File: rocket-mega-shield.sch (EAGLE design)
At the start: 66 parts, among them J1 ExtBatt, J2 Mega R3, J3 XBEE, J4 MICROSD, J5 U.FL, J6 1X6TERMINALBLOCK, Q1 SI7112DN, Q2 BSS138, Q3 BSS138, Q4 SI7112DN, Q5 SI7112DN, Q6 SI7112DN, Q7 SI7112DN, U1 NCP1117DT33G, U2 M74HC4050M, U3 FGPMMOPA6H, U4 BMP180, U5 LSM303DLHCTR, U6 L3GD20TR, U7 ADXL377

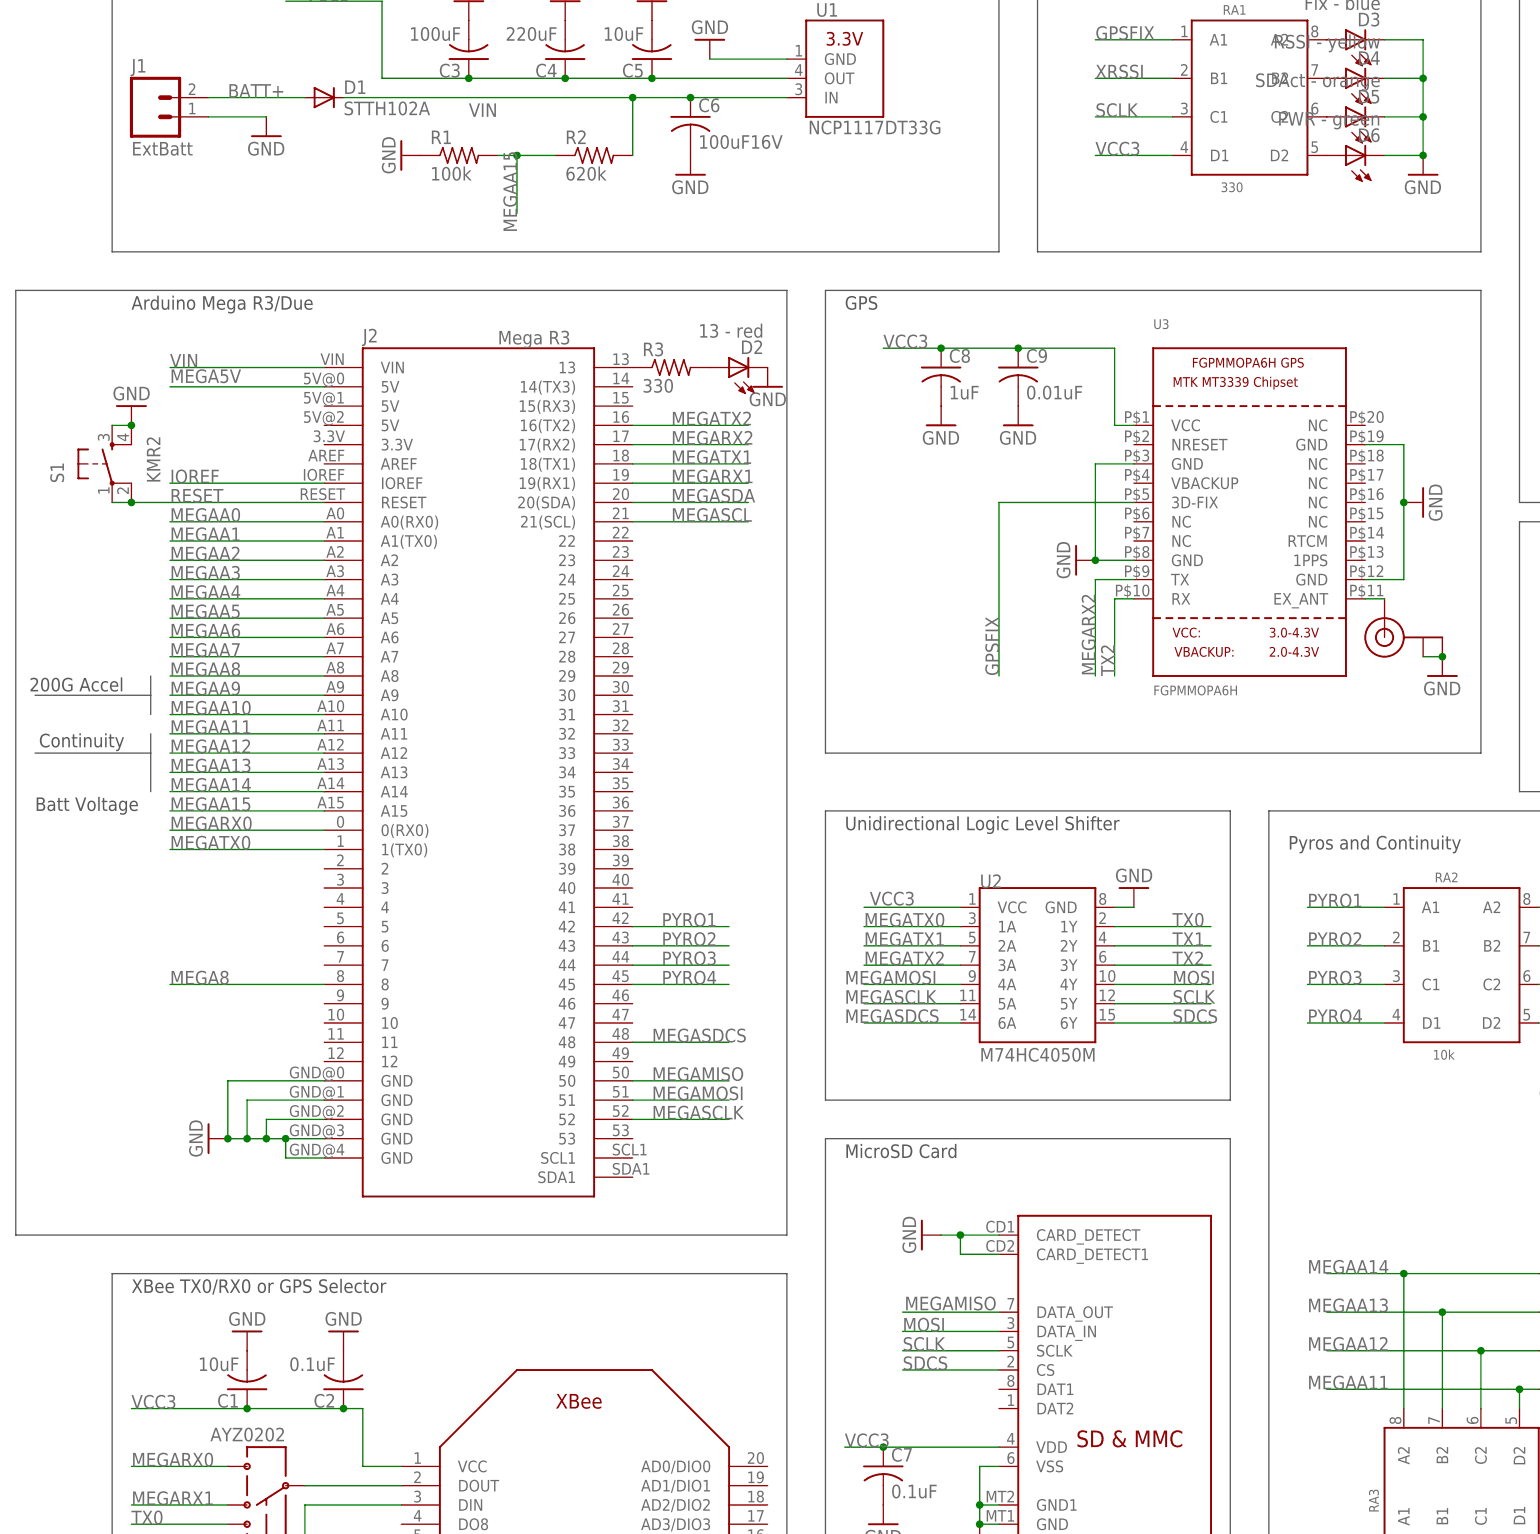
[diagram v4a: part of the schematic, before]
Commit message: moving pins around to match the Due pin availablility
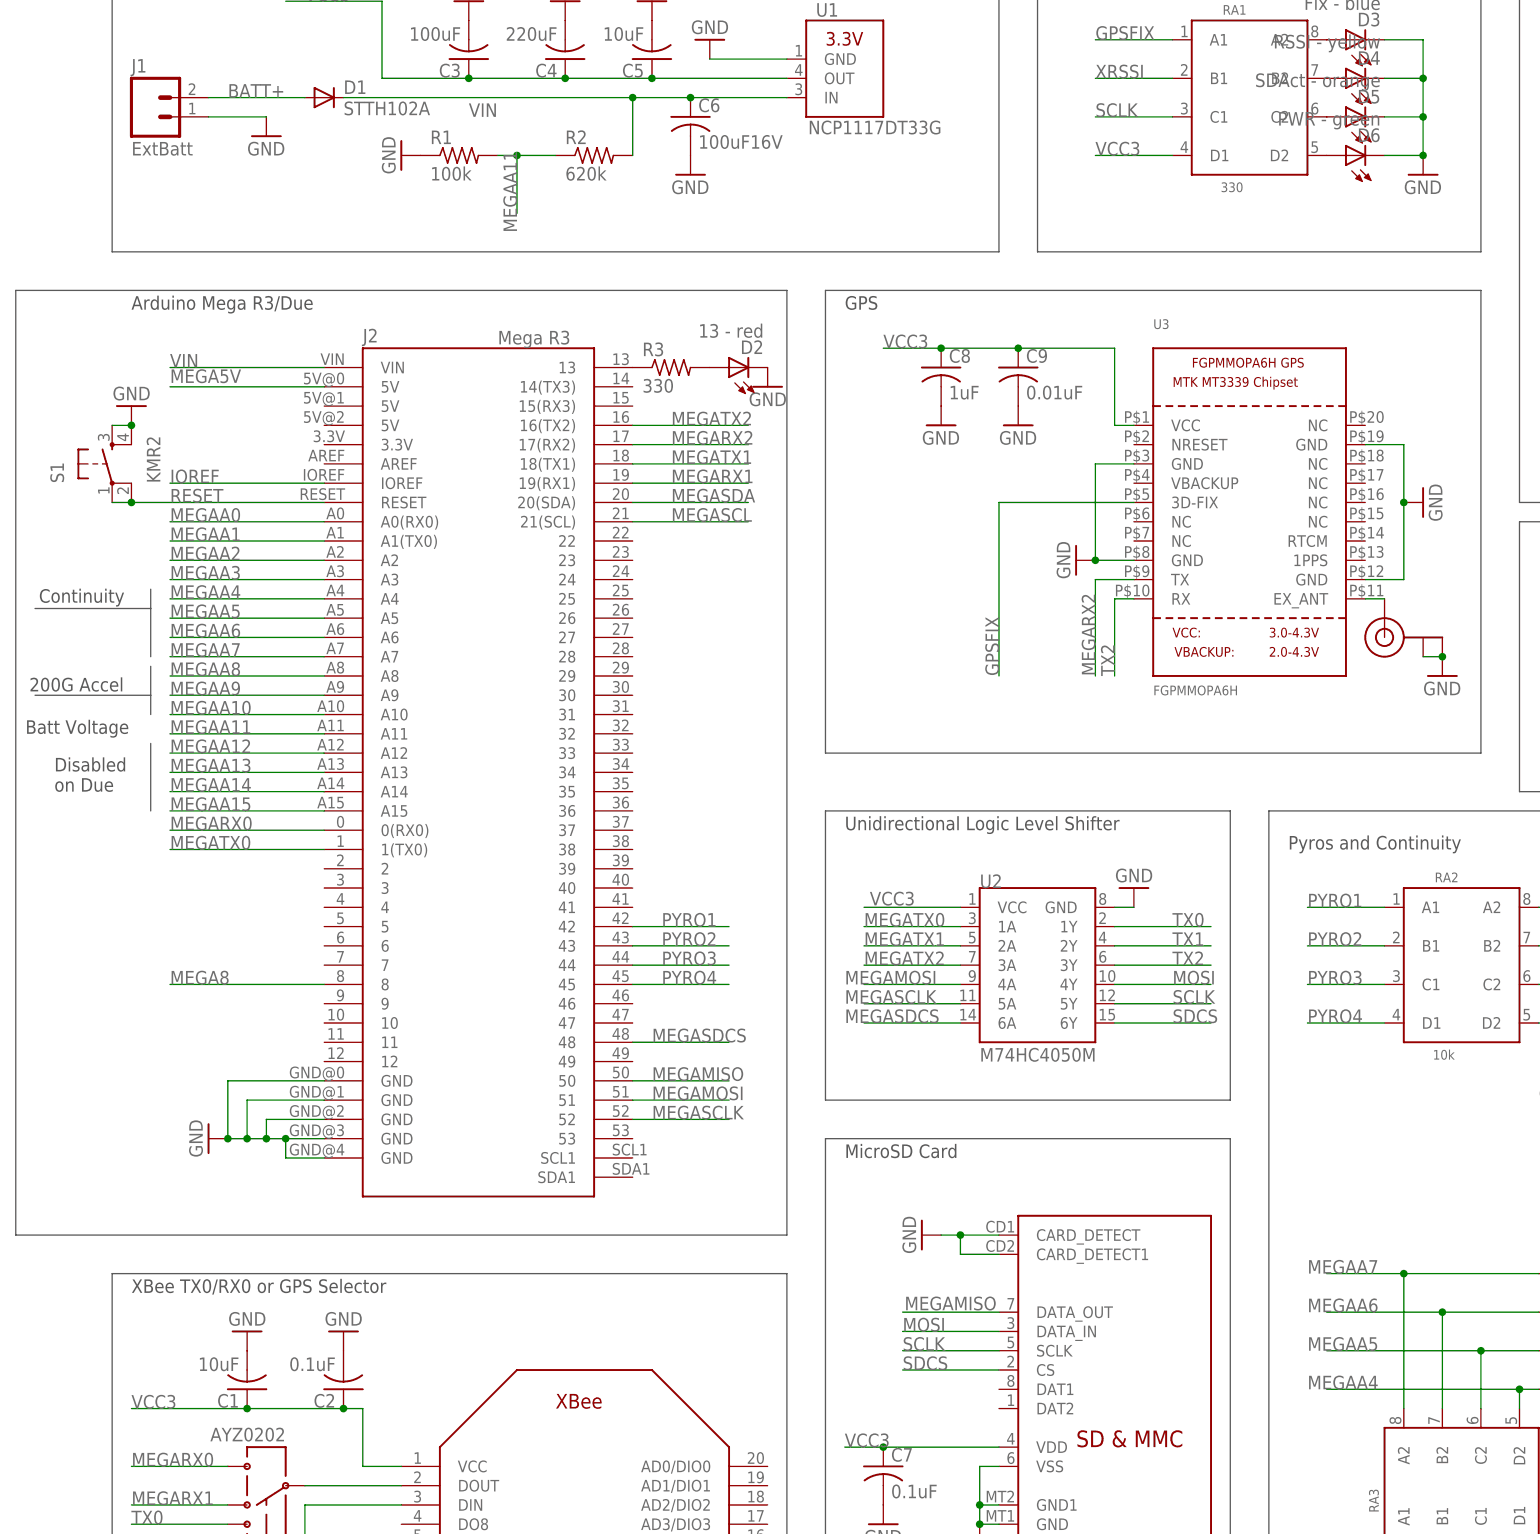
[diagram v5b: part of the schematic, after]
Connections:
- net MEGAA11: now also R1.2, R2.1; no longer RA3.D2, RA4.D1
- net MEGAA12: no longer RA3.C2, RA4.C1
- net MEGAA13: no longer RA3.B2, RA4.B1
- net MEGAA14: no longer RA3.A2, RA4.A1
- net MEGAA15: no longer R1.2, R2.1
- net MEGAA4: now also RA3.D2, RA4.D1
- net MEGAA5: now also RA3.C2, RA4.C1
- net MEGAA6: now also RA3.B2, RA4.B1
- net MEGAA7: now also RA3.A2, RA4.A1
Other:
- note added: "Disabled on Due"
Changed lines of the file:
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@@
 <wire x1="27.94" y1="114.3" x2="-30.48" y2="114.3" width="0.1524" layer="97"/>
 <text x="-27.94" y="109.22" size="1.778" layer="97">LED Bank 1</text>
-<wire x1="-147.32" y1="15.24" x2="-147.32" y2="12.7" width="0.1524" layer="97"/>
+<wire x1="-147.32" y1="16.51" x2="-147.32" y2="12.7" width="0.1524" layer="97"/>
 <wire x1="-147.32" y1="12.7" x2="-147.32" y2="10.16" width="0.1524" layer="97"/>
 <wire x1="-162.56" y1="12.7" x2="-147.32" y2="12.7" width="0.1524" layer="97"/>
 <text x="-163.322" y="13.208" size="1.778" layer="97">200G Accel</text>
-<wire x1="-147.32" y1="7.62" x2="-147.32" y2="5.08" width="0.1524" layer="97"/>
-<wire x1="-147.32" y1="5.08" x2="-147.32" y2="0" width="0.1524" layer="97"/>
-<wire x1="-147.32" y1="5.08" x2="-162.56" y2="5.08" width="0.1524" layer="97"/>
-<text x="-162.052" y="5.842" size="1.778" layer="97">Continuity</text>
-<text x="-162.56" y="-2.54" size="1.778" layer="97">Batt Voltage</text>
+<wire x1="-147.32" y1="26.67" x2="-147.32" y2="24.13" width="0.1524" layer="97"/>
+<wire x1="-147.32" y1="24.13" x2="-147.32" y2="17.78" width="0.1524" layer="97"/>
+<wire x1="-147.32" y1="24.13" x2="-162.56" y2="24.13" width="0.1524" layer="97"/>
+<text x="-162.052" y="24.892" size="1.778" layer="97">Continuity</text>
+<text x="-163.83" y="7.62" size="1.778" layer="97">Batt Voltage</text>
 <text x="35.56" y="33.02" size="1.778" layer="97">Buzzer</text>
 <wire x1="33.02" y1="35.56" x2="33.02" y2="0" width="0.1524" layer="97"/>
@@
 <text x="-140.97" y="121.92" size="1.778" layer="97" font="vector">Designed by Kurtis Kopf</text>
 <text x="-140.97" y="119.38" size="1.778" layer="97" font="vector">OpenSourceAerospace.com</text>
+<wire x1="-147.32" y1="6.35" x2="-147.32" y2="-2.54" width="0.1524" layer="97"/>
+<text x="-160.02" y="0" size="1.778" layer="97">Disabled
+on Due</text>
 </plain>
 <instances>
@@
 <label x="-144.78" y="25.4" size="1.778" layer="95"/>
 </segment>
+<segment>
+<pinref part="RA4" gate="G$1" pin="D1"/>
+<wire x1="35.56" y1="-78.74" x2="33.02" y2="-78.74" width="0.1524" layer="91"/>
+<pinref part="RA3" gate="G$1" pin="D2"/>
+<wire x1="33.02" y1="-78.74" x2="7.62" y2="-78.74" width="0.1524" layer="91"/>
+<wire x1="33.02" y1="-81.28" x2="33.02" y2="-78.74" width="0.1524" layer="91"/>
+<junction x="33.02" y="-78.74"/>
+<label x="5.08" y="-78.74" size="1.778" layer="95"/>
+</segment>
 </net>
 <net name="MEGAA5" class="0">
@@
 <label x="-144.78" y="22.86" size="1.778" layer="95"/>
 </segment>
+<segment>
+<pinref part="RA4" gate="G$1" pin="C1"/>
+<wire x1="35.56" y1="-73.66" x2="27.94" y2="-73.66" width="0.1524" layer="91"/>
+<pinref part="RA3" gate="G$1" pin="C2"/>
+<wire x1="27.94" y1="-73.66" x2="7.62" y2="-73.66" width="0.1524" layer="91"/>
+<wire x1="27.94" y1="-81.28" x2="27.94" y2="-73.66" width="0.1524" layer="91"/>
+<junction x="27.94" y="-73.66"/>
+<label x="5.08" y="-73.66" size="1.778" layer="95"/>
+</segment>
 </net>
 <net name="MEGAA6" class="0">
@@
 <wire x1="-124.46" y1="20.32" x2="-144.78" y2="20.32" width="0.1524" layer="91"/>
 <label x="-144.78" y="20.32" size="1.778" layer="95"/>
+</segment>
+<segment>
+<pinref part="RA4" gate="G$1" pin="B1"/>
+<wire x1="35.56" y1="-68.58" x2="22.86" y2="-68.58" width="0.1524" layer="91"/>
+<pinref part="RA3" gate="G$1" pin="B2"/>
+<wire x1="22.86" y1="-68.58" x2="7.62" y2="-68.58" width="0.1524" layer="91"/>
+<wire x1="22.86" y1="-81.28" x2="22.86" y2="-68.58" width="0.1524" layer="91"/>
+<junction x="22.86" y="-68.58"/>
+<label x="5.08" y="-68.58" size="1.778" layer="95"/>
 </segment>
 </net>
@@
 <wire x1="-124.46" y1="17.78" x2="-144.78" y2="17.78" width="0.1524" layer="91"/>
 <label x="-144.78" y="17.78" size="1.778" layer="95"/>
+</segment>
+<segment>
+<pinref part="RA4" gate="G$1" pin="A1"/>
+<wire x1="35.56" y1="-63.5" x2="17.78" y2="-63.5" width="0.1524" layer="91"/>
+<pinref part="RA3" gate="G$1" pin="A2"/>
+<wire x1="17.78" y1="-63.5" x2="7.62" y2="-63.5" width="0.1524" layer="91"/>
+<wire x1="17.78" y1="-81.28" x2="17.78" y2="-63.5" width="0.1524" layer="91"/>
+<junction x="17.78" y="-63.5"/>
+<label x="5.08" y="-63.5" size="1.778" layer="95"/>
 </segment>
 </net>
@@
 </segment>
 <segment>
-<pinref part="RA4" gate="G$1" pin="D1"/>
-<wire x1="35.56" y1="-78.74" x2="33.02" y2="-78.74" width="0.1524" layer="91"/>
-<pinref part="RA3" gate="G$1" pin="D2"/>
-<wire x1="33.02" y1="-78.74" x2="7.62" y2="-78.74" width="0.1524" layer="91"/>
-<wire x1="33.02" y1="-81.28" x2="33.02" y2="-78.74" width="0.1524" layer="91"/>
-<junction x="33.02" y="-78.74"/>
-<label x="5.08" y="-78.74" size="1.778" layer="95"/>
-</segment>
-</net>
-<net name="MEGAA12" class="0">
-<segment>
-<pinref part="J2" gate="G$1" pin="A12"/>
-<wire x1="-124.46" y1="5.08" x2="-144.78" y2="5.08" width="0.1524" layer="91"/>
-<label x="-144.78" y="5.08" size="1.778" layer="95"/>
-</segment>
-<segment>
-<pinref part="RA4" gate="G$1" pin="C1"/>
-<wire x1="35.56" y1="-73.66" x2="27.94" y2="-73.66" width="0.1524" layer="91"/>
-<pinref part="RA3" gate="G$1" pin="C2"/>
-<wire x1="27.94" y1="-73.66" x2="7.62" y2="-73.66" width="0.1524" layer="91"/>
-<wire x1="27.94" y1="-81.28" x2="27.94" y2="-73.66" width="0.1524" layer="91"/>
-<junction x="27.94" y="-73.66"/>
-<label x="5.08" y="-73.66" size="1.778" layer="95"/>
-</segment>
-</net>
-<net name="MEGAA13" class="0">
-<segment>
-<pinref part="J2" gate="G$1" pin="A13"/>
-<wire x1="-124.46" y1="2.54" x2="-144.78" y2="2.54" width="0.1524" layer="91"/>
-<label x="-144.78" y="2.54" size="1.778" layer="95"/>
-</segment>
-<segment>
-<pinref part="RA4" gate="G$1" pin="B1"/>
-<wire x1="35.56" y1="-68.58" x2="22.86" y2="-68.58" width="0.1524" layer="91"/>
-<pinref part="RA3" gate="G$1" pin="B2"/>
-<wire x1="22.86" y1="-68.58" x2="7.62" y2="-68.58" width="0.1524" layer="91"/>
-<wire x1="22.86" y1="-81.28" x2="22.86" y2="-68.58" width="0.1524" layer="91"/>
-<junction x="22.86" y="-68.58"/>
-<label x="5.08" y="-68.58" size="1.778" layer="95"/>
-</segment>
-</net>
-<net name="MEGAA14" class="0">
-<segment>
-<pinref part="J2" gate="G$1" pin="A14"/>
-<wire x1="-124.46" y1="0" x2="-144.78" y2="0" width="0.1524" layer="91"/>
-<label x="-144.78" y="0" size="1.778" layer="95"/>
-</segment>
-<segment>
-<pinref part="RA4" gate="G$1" pin="A1"/>
-<wire x1="35.56" y1="-63.5" x2="17.78" y2="-63.5" width="0.1524" layer="91"/>
-<pinref part="RA3" gate="G$1" pin="A2"/>
-<wire x1="17.78" y1="-63.5" x2="7.62" y2="-63.5" width="0.1524" layer="91"/>
-<wire x1="17.78" y1="-81.28" x2="17.78" y2="-63.5" width="0.1524" layer="91"/>
-<junction x="17.78" y="-63.5"/>
-<label x="5.08" y="-63.5" size="1.778" layer="95"/>
-</segment>
-</net>
-<net name="MEGAA15" class="0">
-<segment>
-<pinref part="J2" gate="G$1" pin="A15"/>
-<wire x1="-124.46" y1="-2.54" x2="-144.78" y2="-2.54" width="0.1524" layer="91"/>
-<label x="-144.78" y="-2.54" size="1.778" layer="95"/>
-</segment>
-<segment>
 <pinref part="R1" gate="G$1" pin="2"/>
 <pinref part="R2" gate="G$1" pin="1"/>
@@
 </segment>
 </net>
+<net name="MEGAA12" class="0">
+<segment>
+<pinref part="J2" gate="G$1" pin="A12"/>
+<wire x1="-124.46" y1="5.08" x2="-144.78" y2="5.08" width="0.1524" layer="91"/>
+<label x="-144.78" y="5.08" size="1.778" layer="95"/>
+</segment>
+</net>
+<net name="MEGAA13" class="0">
+<segment>
+<pinref part="J2" gate="G$1" pin="A13"/>
+<wire x1="-124.46" y1="2.54" x2="-144.78" y2="2.54" width="0.1524" layer="91"/>
+<label x="-144.78" y="2.54" size="1.778" layer="95"/>
+</segment>
+</net>
+<net name="MEGAA14" class="0">
+<segment>
+<pinref part="J2" gate="G$1" pin="A14"/>
+<wire x1="-124.46" y1="0" x2="-144.78" y2="0" width="0.1524" layer="91"/>
+<label x="-144.78" y="0" size="1.778" layer="95"/>
+</segment>
+</net>
+<net name="MEGAA15" class="0">
+<segment>
+<pinref part="J2" gate="G$1" pin="A15"/>
+<wire x1="-124.46" y1="-2.54" x2="-144.78" y2="-2.54" width="0.1524" layer="91"/>
+<label x="-144.78" y="-2.54" size="1.778" layer="95"/>
+</segment>
+</net>
 <net name="N$13" class="0">
 <segment>
@@
 </schematic>
 </drawing>
+<compatibility>
+<note version="6.3" minversion="6.2.2" severity="warning">
+Since Version 6.2.2 text objects can contain more than one line,
+which will not be processed correctly with this version.
+</note>
+</compatibility>
 </eagle>
